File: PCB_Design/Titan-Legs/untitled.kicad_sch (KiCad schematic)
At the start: 7 parts

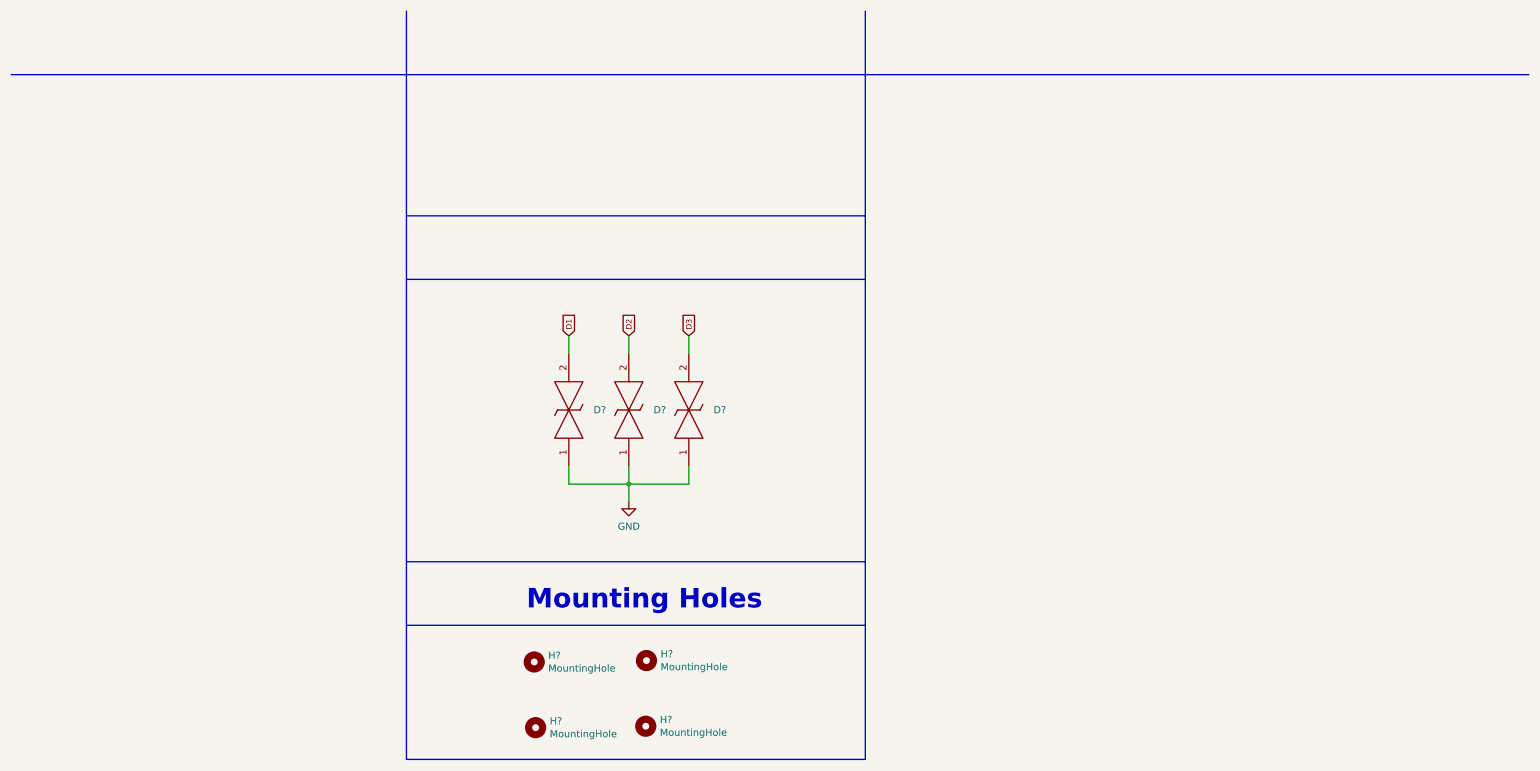
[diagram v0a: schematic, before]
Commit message: schematics 1st iteration completed
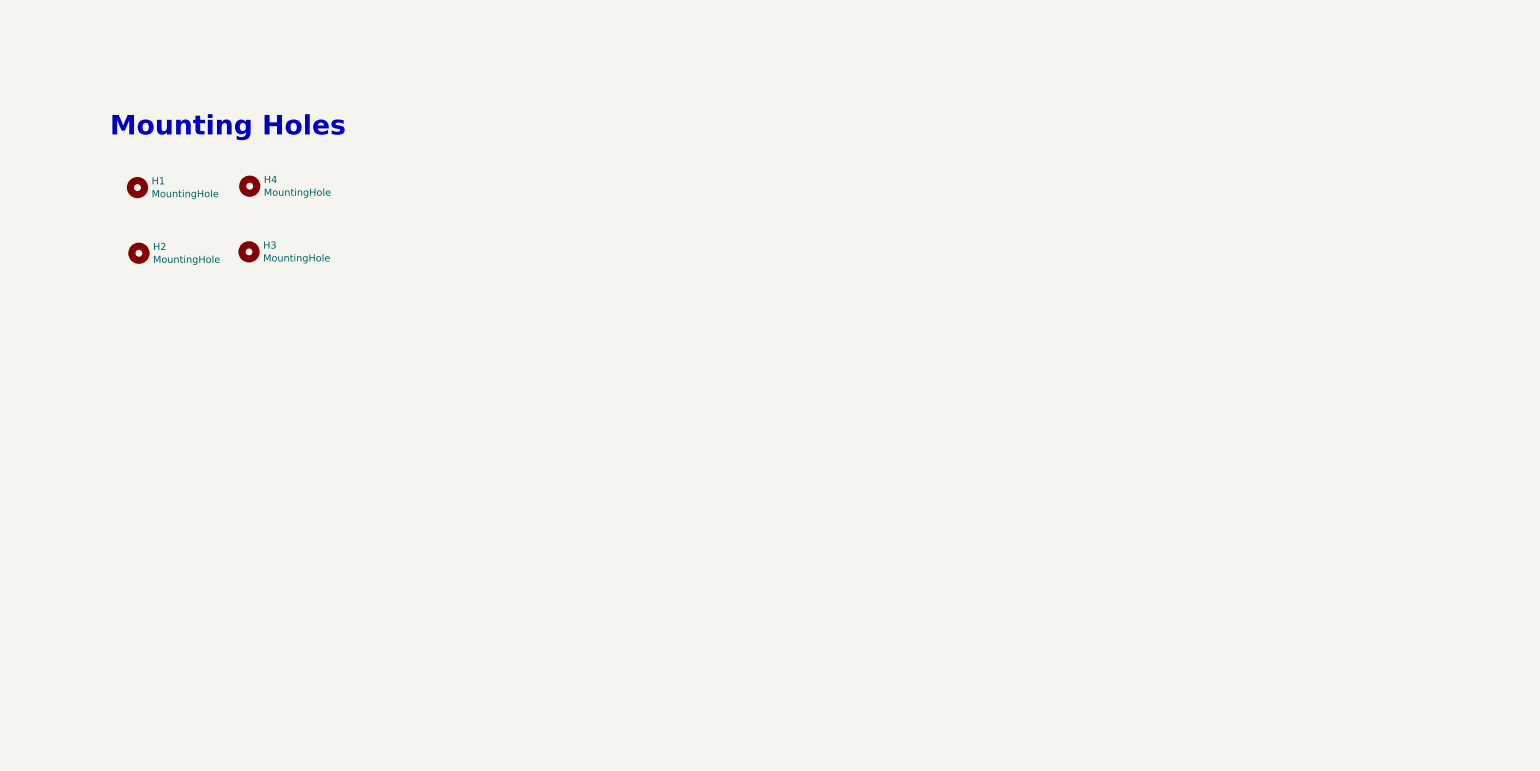
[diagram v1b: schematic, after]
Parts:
- removed D? (x3): LESD5D5.0CT1G, LESD5D50CT1G, symbol USB-UART_LESD5D5.0CT1G:LESD5D5.0CT1G
- gave numbers to parts that had none: 4
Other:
- moved on the sheet: H1, H2, H3, H4

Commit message: updating recent changes
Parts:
- added R10: 4.7K, Resistor_SMD:R_0603_1608Metric, symbol Device:R
- added U5: DS18S20Z+, Temp-Sensor_DS18S20Z_:DS18S20Z_, symbol DS18S20Z_:DS18S20Z+
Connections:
- new net: R10.2, U5.4 (DQ)
- new net 3V3_IN: R10.1, U5.3 (VDD)
- new net GND: U5.5 (GND)
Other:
- note added: "Temperature Sensor"
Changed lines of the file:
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@@
 (kicad_sch (version 20211123) (generator eeschema)
   (paper "A4")
-  (text "Mounting Holes\n" (at 29.21 34.29 0)
+  (polyline (pts (xy 95.758 11.938) (xy 95.758 77.1144))
+    (stroke (width 0) (type default) (color 0 0 0 0))
+  )
+  (wire (pts (xy 112.8268 50.1396) (xy 112.8268 53.7972))
+    (stroke (width 0) (type default) (color 0 0 0 0))
+  )
+  (wire (pts (xy 164.3888 58.8772) (xy 159.004 58.8772))
+    (stroke (width 0) (type default) (color 0 0 0 0))
+  )
+  (wire (pts (xy 120.4468 53.7972) (xy 123.444 53.7972))
+    (stroke (width 0) (type default) (color 0 0 0 0))
+  )
+  (polyline (pts (xy 12.0904 77.1144) (xy 95.758 77.1144))
+    (stroke (width 0) (type default) (color 0 0 0 0))
+  )
+  (wire (pts (xy 164.3888 60.452) (xy 164.3888 58.8772))
+    (stroke (width 0) (type default) (color 0 0 0 0))
+  )
+  (wire (pts (xy 159.004 48.7172) (xy 164.1856 48.7172))
+    (stroke (width 0) (type default) (color 0 0 0 0))
+  )
+  (text "Temperature Sensor" (at 114.2492 31.3436 0)
     (effects (font (size 3.5 3.5) bold) (justify left bottom))
+  )
+  (text "Mounting Holes\n" (at 30.2768 31.0388 0)
+    (effects (font (size 3.5 3.5) bold) (justify left bottom))
+  )
+  (global_label "3V3_IN" (shape input) (at 164.1856 48.7172 0) (fields_autoplaced)
+    (effects (font (size 1 1)) (justify left))
+    (property "Intersheet References" "${INTERSHEET_REFS}" (id 0) (at 171.1332 48.6547 0)
+      (effects (font (size 1 1)) (justify left) hide)
+    )
+  )
+  (global_label "3V3_IN" (shape input) (at 112.8268 50.1396 90) (fields_autoplaced)
+    (effects (font (size 1 1)) (justify left))
+    (property "Intersheet References" "${INTERSHEET_REFS}" (id 0) (at 112.7643 43.192 90)
+      (effects (font (size 1 1)) (justify left) hide)
+    )
   )
   (symbol (lib_id "Mechanical:MountingHole") (at 34.163 43.18 0) (unit 1)
@@
     )
   )
+  (symbol (lib_id "Device:R") (at 116.6368 53.7972 90) (unit 1)
+    (in_bom yes) (on_board yes)
+    (property "Reference" "R10" (id 0) (at 116.6368 51.7144 90)
+      (effects (font (size 1 1)))
+    )
+    (property "Value" "4.7K" (id 1) (at 116.6368 53.7972 90)
+      (effects (font (size 1 1)))
+    )
+    (property "Footprint" "Resistor_SMD:R_0603_1608Metric" (id 2) (at 116.6368 55.5752 90)
+      (effects (font (size 1.27 1.27)) hide)
+    )
+    (property "Datasheet" "~" (id 3) (at 116.6368 53.7972 0)
+      (effects (font (size 1.27 1.27)) hide)
+    )
+    (pin "1")
+    (pin "2")
+  )
+  (symbol (lib_id "power:GND") (at 164.3888 60.452 0) (unit 1)
+    (in_bom yes) (on_board yes)
+    (property "Reference" "#PWR032" (id 0) (at 164.3888 66.802 0)
+      (effects (font (size 1.27 1.27)) hide)
+    )
+    (property "Value" "GND" (id 1) (at 164.4904 64.3636 0))
+    (property "Footprint" "" (id 2) (at 164.3888 60.452 0)
+      (effects (font (size 1.27 1.27)) hide)
+    )
+    (property "Datasheet" "" (id 3) (at 164.3888 60.452 0)
+      (effects (font (size 1.27 1.27)) hide)
+    )
+    (pin "1")
+  )
+  (symbol (lib_id "DS18S20Z_:DS18S20Z+") (at 141.224 53.7972 0) (unit 1)
+    (in_bom yes) (on_board yes) (fields_autoplaced)
+    (property "Reference" "U5" (id 0) (at 141.224 40.5384 0))
+    (property "Value" "DS18S20Z+" (id 1) (at 141.224 43.0784 0))
+    (property "Footprint" "Temp-Sensor_DS18S20Z_:DS18S20Z_" (id 2) (at 141.224 53.7972 0)
+      (effects (font (size 1.27 1.27)) (justify left bottom) hide)
+    )
+    (property "Datasheet" "" (id 3) (at 141.224 53.7972 0)
+      (effects (font (size 1.27 1.27)) (justify left bottom) hide)
+    )
+    (property "PARTREV" "3" (id 4) (at 141.224 53.7972 0)
+      (effects (font (size 1.27 1.27)) (justify left bottom) hide)
+    )
+    (property "STANDARD" "IPC7351B" (id 5) (at 141.224 53.7972 0)
+      (effects (font (size 1.27 1.27)) (justify left bottom) hide)
+    )
+    (property "MANUFACTURER" "Maxim Integrated" (id 6) (at 141.224 53.7972 0)
+      (effects (font (size 1.27 1.27)) (justify left bottom) hide)
+    )
+    (pin "3")
+    (pin "4")
+    (pin "5")
+  )
   (symbol (lib_id "Mechanical:MountingHole") (at 34.417 54.991 0) (unit 1)

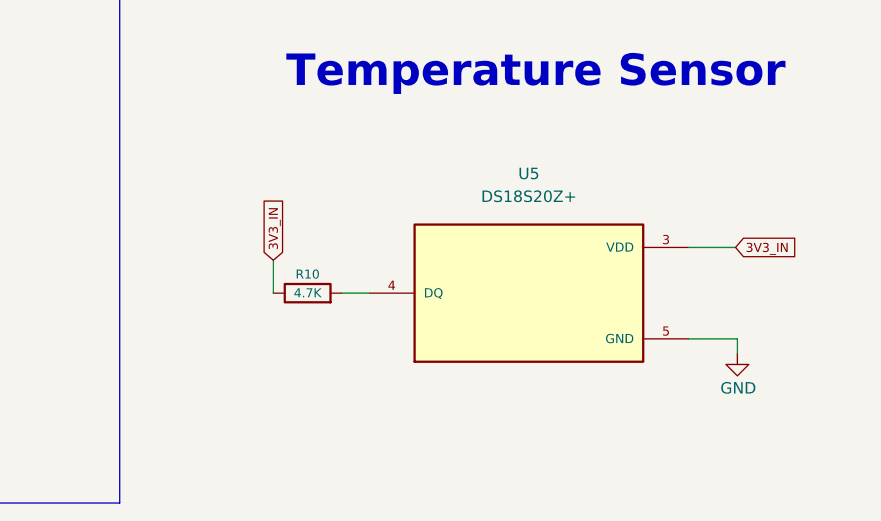
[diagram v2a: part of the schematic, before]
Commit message: Add new placement for Quadruped PCB
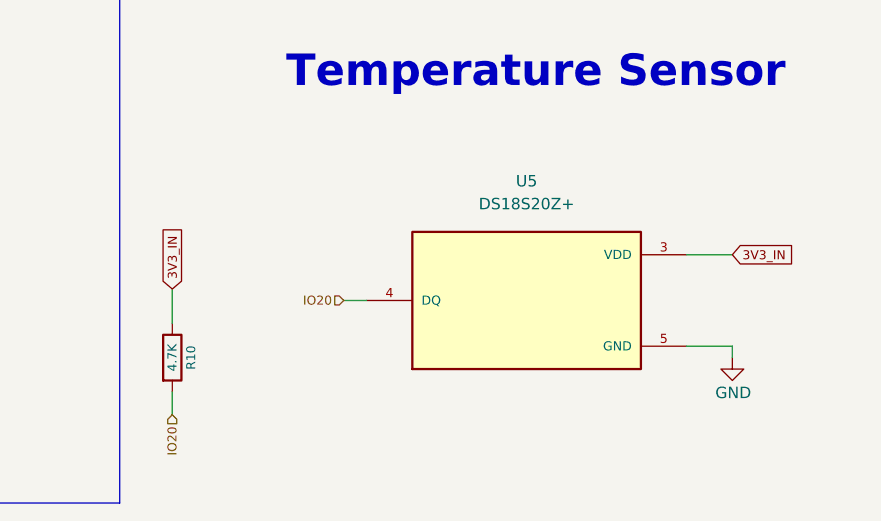
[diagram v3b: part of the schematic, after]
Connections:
- net IO20: now reaches R10.2, U5.4 (DQ)
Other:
- moved on the sheet: R10, U5
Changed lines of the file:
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@@
     (stroke (width 0) (type default) (color 0 0 0 0))
   )
-  (wire (pts (xy 112.8268 50.1396) (xy 112.8268 53.7972))
+  (wire (pts (xy 101.6 64.77) (xy 101.6 67.31))
     (stroke (width 0) (type default) (color 0 0 0 0))
   )
-  (wire (pts (xy 164.3888 58.8772) (xy 159.004 58.8772))
+  (wire (pts (xy 101.6 53.34) (xy 101.6 57.15))
     (stroke (width 0) (type default) (color 0 0 0 0))
   )
-  (wire (pts (xy 120.4468 53.7972) (xy 123.444 53.7972))
+  (wire (pts (xy 158.75 49.53) (xy 163.83 49.53))
+    (stroke (width 0) (type default) (color 0 0 0 0))
+  )
+  (wire (pts (xy 120.65 54.61) (xy 123.19 54.61))
+    (stroke (width 0) (type default) (color 0 0 0 0))
+  )
+  (wire (pts (xy 158.75 59.69) (xy 163.83 59.69))
+    (stroke (width 0) (type default) (color 0 0 0 0))
+  )
+  (wire (pts (xy 163.83 59.69) (xy 163.83 60.96))
     (stroke (width 0) (type default) (color 0 0 0 0))
   )
   (polyline (pts (xy 12.0904 77.1144) (xy 95.758 77.1144))
-    (stroke (width 0) (type default) (color 0 0 0 0))
-  )
-  (wire (pts (xy 164.3888 60.452) (xy 164.3888 58.8772))
-    (stroke (width 0) (type default) (color 0 0 0 0))
-  )
-  (wire (pts (xy 159.004 48.7172) (xy 164.1856 48.7172))
     (stroke (width 0) (type default) (color 0 0 0 0))
   )
@@
     (effects (font (size 3.5 3.5) bold) (justify left bottom))
   )
-  (global_label "3V3_IN" (shape input) (at 164.1856 48.7172 0) (fields_autoplaced)
+  (global_label "3V3_IN" (shape input) (at 163.83 49.53 0) (fields_autoplaced)
     (effects (font (size 1 1)) (justify left))
-    (property "Intersheet References" "${INTERSHEET_REFS}" (id 0) (at 171.1332 48.6547 0)
+    (property "Intersheet References" "${INTERSHEET_REFS}" (id 0) (at 170.7776 49.4675 0)
       (effects (font (size 1 1)) (justify left) hide)
     )
   )
-  (global_label "3V3_IN" (shape input) (at 112.8268 50.1396 90) (fields_autoplaced)
+  (global_label "3V3_IN" (shape input) (at 101.6 53.34 90) (fields_autoplaced)
     (effects (font (size 1 1)) (justify left))
-    (property "Intersheet References" "${INTERSHEET_REFS}" (id 0) (at 112.7643 43.192 90)
+    (property "Intersheet References" "${INTERSHEET_REFS}" (id 0) (at 101.5375 46.3924 90)
       (effects (font (size 1 1)) (justify left) hide)
     )
+  )
+  (hierarchical_label "IO20" (shape input) (at 101.6 67.31 270)
+    (effects (font (size 1 1)) (justify right))
+  )
+  (hierarchical_label "IO20" (shape input) (at 120.65 54.61 180)
+    (effects (font (size 1 1)) (justify right))
   )
   (symbol (lib_id "Mechanical:MountingHole") (at 34.163 43.18 0) (unit 1)
@@
     )
   )
-  (symbol (lib_id "Device:R") (at 116.6368 53.7972 90) (unit 1)
+  (symbol (lib_id "Device:R") (at 101.6 60.96 0) (unit 1)
     (in_bom yes) (on_board yes)
-    (property "Reference" "R10" (id 0) (at 116.6368 51.7144 90)
+    (property "Reference" "R10" (id 0) (at 103.6828 60.96 90)
       (effects (font (size 1 1)))
     )
-    (property "Value" "4.7K" (id 1) (at 116.6368 53.7972 90)
+    (property "Value" "4.7K" (id 1) (at 101.6 60.96 90)
       (effects (font (size 1 1)))
     )
-    (property "Footprint" "Resistor_SMD:R_0603_1608Metric" (id 2) (at 116.6368 55.5752 90)
+    (property "Footprint" "Resistor_SMD:R_0603_1608Metric" (id 2) (at 99.822 60.96 90)
       (effects (font (size 1.27 1.27)) hide)
     )
-    (property "Datasheet" "~" (id 3) (at 116.6368 53.7972 0)
+    (property "Datasheet" "~" (id 3) (at 101.6 60.96 0)
       (effects (font (size 1.27 1.27)) hide)
     )
@@
     (pin "2")
   )
-  (symbol (lib_id "power:GND") (at 164.3888 60.452 0) (unit 1)
+  (symbol (lib_id "power:GND") (at 163.83 60.96 0) (unit 1)
     (in_bom yes) (on_board yes)
-    (property "Reference" "#PWR032" (id 0) (at 164.3888 66.802 0)
+    (property "Reference" "#PWR032" (id 0) (at 163.83 67.31 0)
       (effects (font (size 1.27 1.27)) hide)
     )
-    (property "Value" "GND" (id 1) (at 164.4904 64.3636 0))
-    (property "Footprint" "" (id 2) (at 164.3888 60.452 0)
+    (property "Value" "GND" (id 1) (at 163.9316 64.8716 0))
+    (property "Footprint" "" (id 2) (at 163.83 60.96 0)
       (effects (font (size 1.27 1.27)) hide)
     )
-    (property "Datasheet" "" (id 3) (at 164.3888 60.452 0)
+    (property "Datasheet" "" (id 3) (at 163.83 60.96 0)
       (effects (font (size 1.27 1.27)) hide)
     )
     (pin "1")
   )
-  (symbol (lib_id "DS18S20Z_:DS18S20Z+") (at 141.224 53.7972 0) (unit 1)
+  (symbol (lib_id "DS18S20Z_:DS18S20Z+") (at 140.97 54.61 0) (unit 1)
     (in_bom yes) (on_board yes) (fields_autoplaced)
-    (property "Reference" "U5" (id 0) (at 141.224 40.5384 0))
-    (property "Value" "DS18S20Z+" (id 1) (at 141.224 43.0784 0))
-    (property "Footprint" "Temp-Sensor_DS18S20Z_:DS18S20Z_" (id 2) (at 141.224 53.7972 0)
+    (property "Reference" "U5" (id 0) (at 140.97 41.3512 0))
+    (property "Value" "DS18S20Z+" (id 1) (at 140.97 43.8912 0))
+    (property "Footprint" "Temp-Sensor_DS18S20Z_:DS18S20Z_" (id 2) (at 140.97 54.61 0)
       (effects (font (size 1.27 1.27)) (justify left bottom) hide)
     )
-    (property "Datasheet" "" (id 3) (at 141.224 53.7972 0)
+    (property "Datasheet" "" (id 3) (at 140.97 54.61 0)
       (effects (font (size 1.27 1.27)) (justify left bottom) hide)
     )
-    (property "PARTREV" "3" (id 4) (at 141.224 53.7972 0)
+    (property "PARTREV" "3" (id 4) (at 140.97 54.61 0)
       (effects (font (size 1.27 1.27)) (justify left bottom) hide)
     )
-    (property "STANDARD" "IPC7351B" (id 5) (at 141.224 53.7972 0)
+    (property "STANDARD" "IPC7351B" (id 5) (at 140.97 54.61 0)
       (effects (font (size 1.27 1.27)) (justify left bottom) hide)
     )
-    (property "MANUFACTURER" "Maxim Integrated" (id 6) (at 141.224 53.7972 0)
+    (property "MANUFACTURER" "Maxim Integrated" (id 6) (at 140.97 54.61 0)
       (effects (font (size 1.27 1.27)) (justify left bottom) hide)
     )
